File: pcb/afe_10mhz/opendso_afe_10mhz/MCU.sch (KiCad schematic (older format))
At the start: 14 parts, among them IC23 STM32G070C

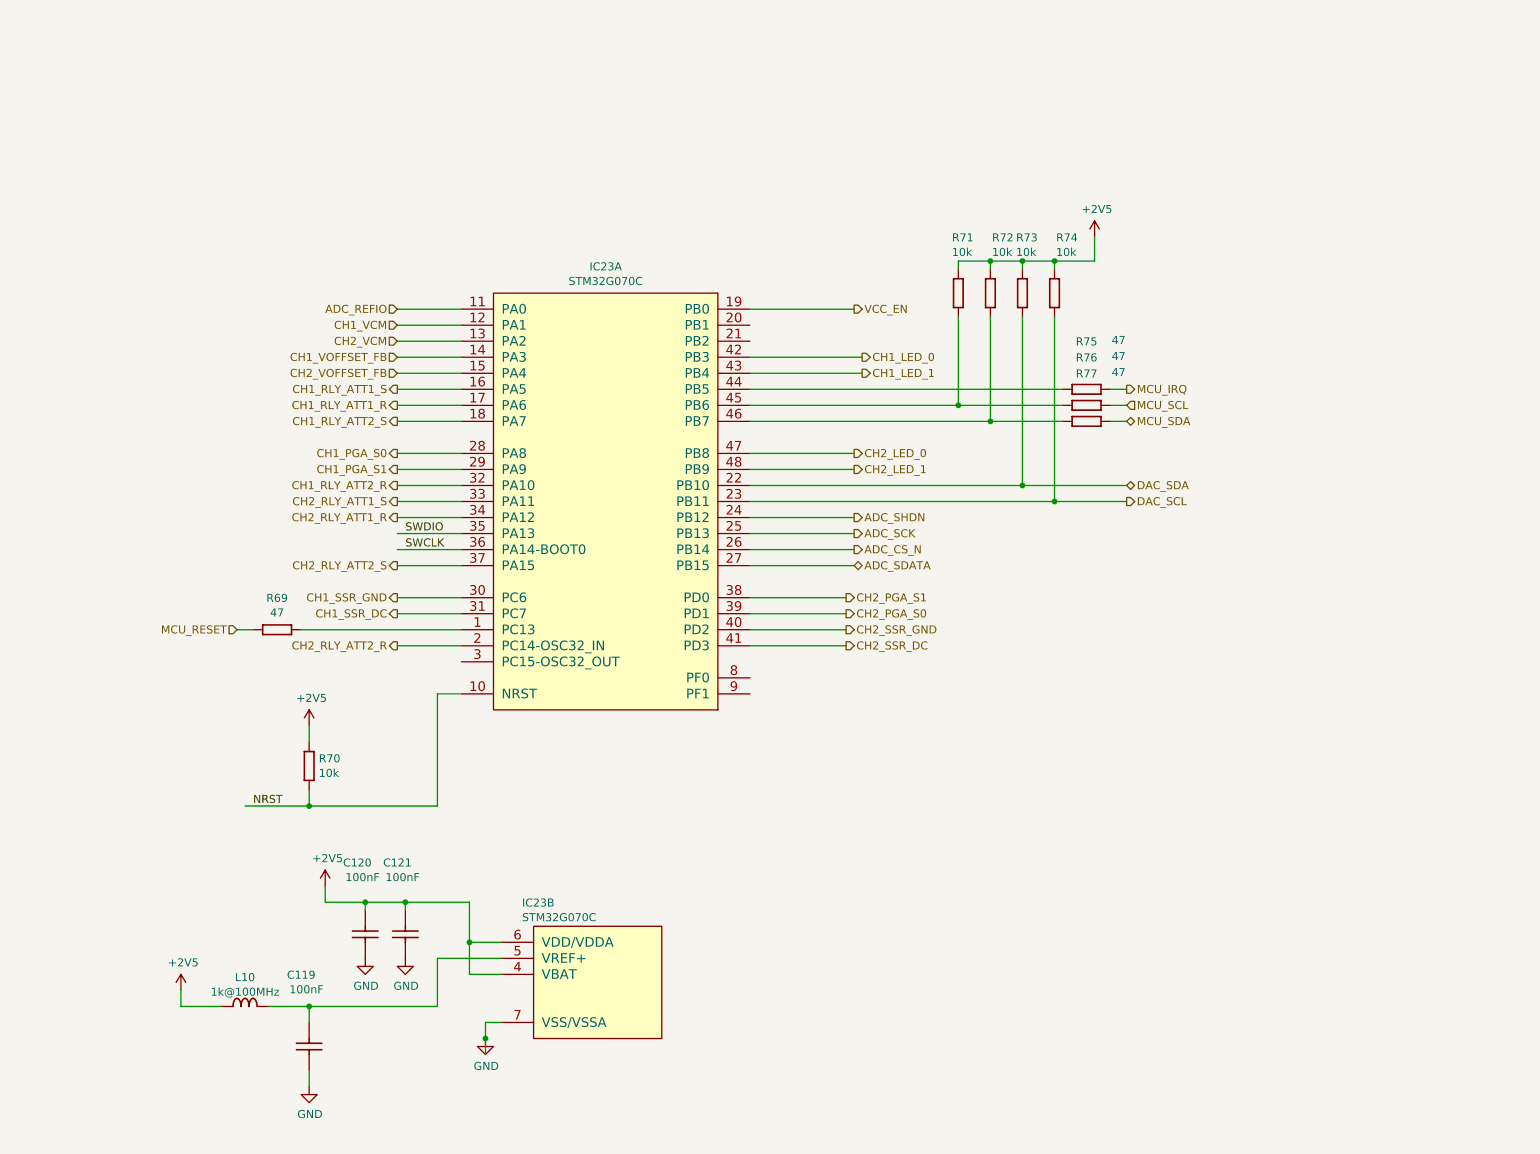
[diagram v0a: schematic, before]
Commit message: AFE schematic: finished port to KiCad
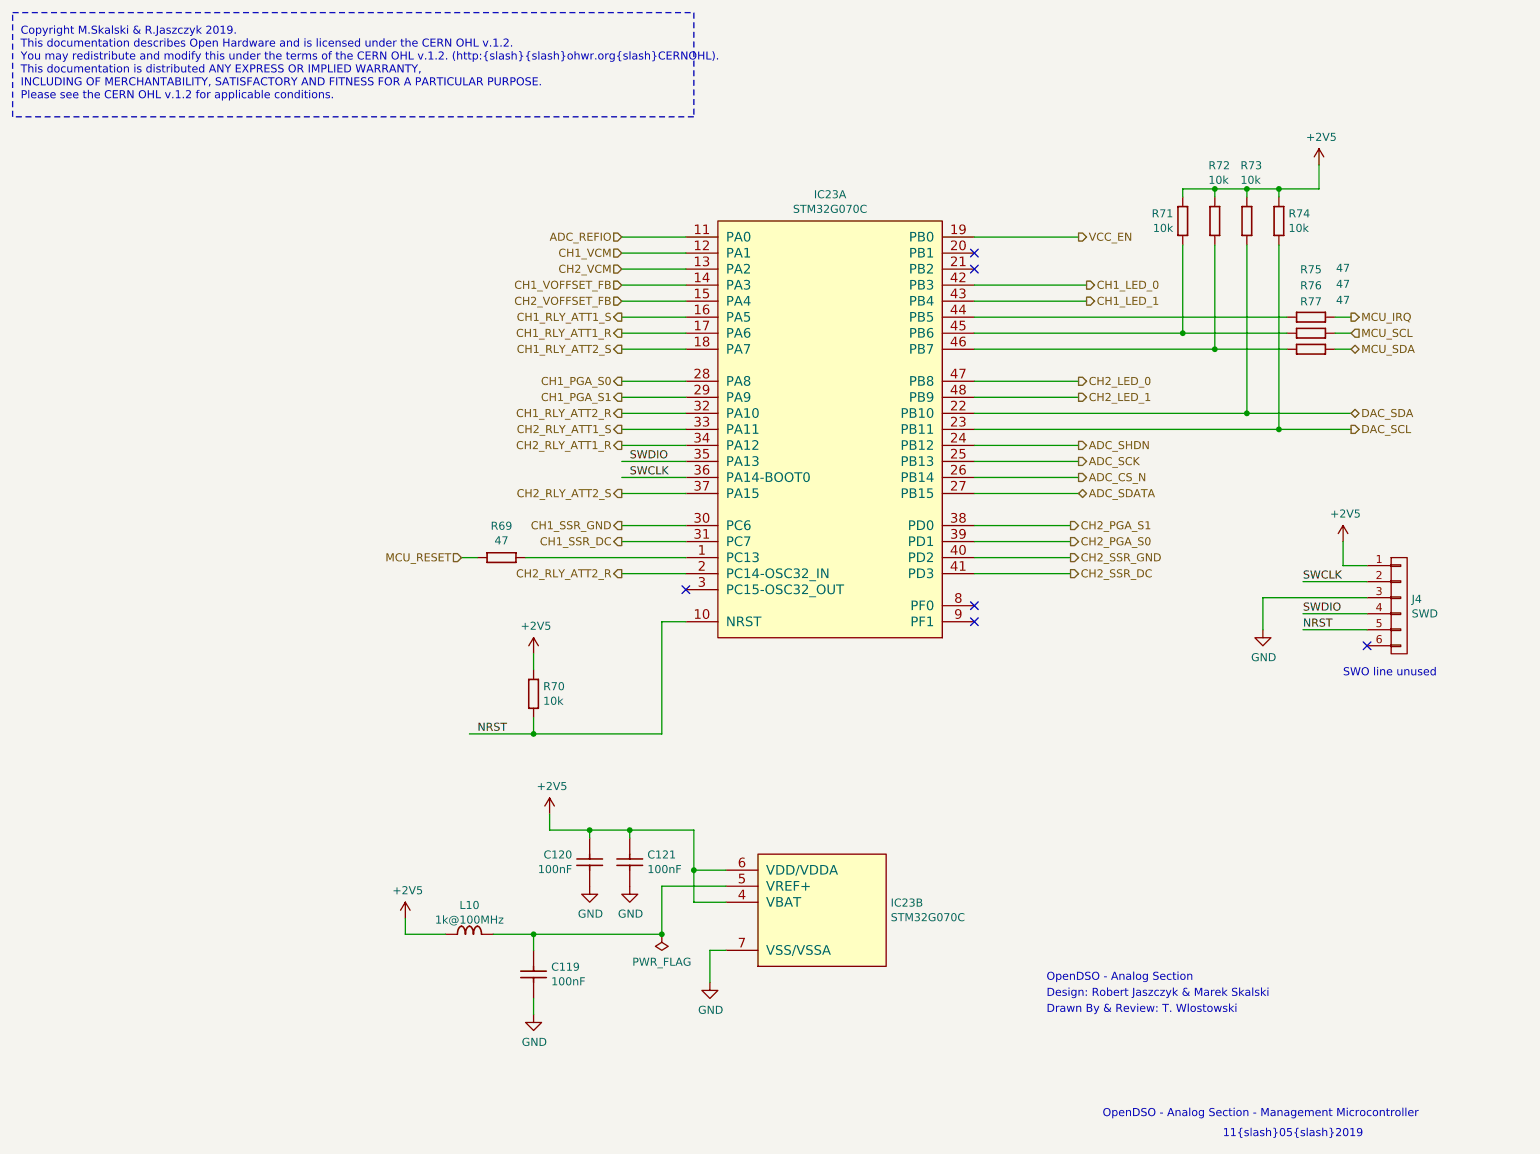
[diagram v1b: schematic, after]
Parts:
- added J4: SWD, Connector_PinHeader_2.54mm:PinHeader_1x06_P2.54mm_Vertical, symbol conn:CONN_01X06
- C119, C120, C121: footprint CAPC1608X87N -> Capacitors SMD:CAPC1608X87N
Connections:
- wire segments 86 -> 92
- no-connect marks 0 -> 6
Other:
- note added: "11/05/2019\n"
- note added: "Copyright M.Skalski & R.Jaszczyk 2019.\nThis documentation describes Open Hardware and is licensed under the CERN OHL v.1.2.\nYou may redistribute and modify this under the terms of the CERN OHL v.1.2. (http://ohwr.org/CERNOHL).\nThis documentation is distributed ANY EXPRESS OR IMPLIED WARRANTY,\nINCLUDING OF MERCHANTABILITY, SATISFACTORY AND FITNESS FOR A PARTICULAR PURPOSE.\nP…"
- note added: "Design: Robert Jaszczyk & Marek Skalski\n"
- note added: "Drawn By & Review: T. Wlostowski\n"
- note added: "OpenDSO - Analog Section - Management Microcontroller"
- note added: "OpenDSO - Analog Section\n"
- note added: "SWO line unused"
- moved on the sheet: C119, C120, C121, IC23A, IC23B, L10, R69, R70, R71, R72, R73, R74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
